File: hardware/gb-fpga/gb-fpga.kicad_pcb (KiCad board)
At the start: 4 copper layers, 80.1 x 78.6 mm, 136 parts, among them J1 USB_C_Receptacle_USB2.0, J2 Cartridge-32pin, J3 BAT+, J4 BAT-, J5 Conn_02x25_Counter_Clockwise, Q1 MBT3904DW1, SW1 Switch, U1 xc7s25ftgb196, U2 MX25R3235FZBxx1, U3 FT2232HQ, U4 LTC3555, U5 TLV61046ADB, U6 TXS0108E, U7 TXS0108E, U8 TXS0108E, U9 TXS0108E, X1 SG-8002JA

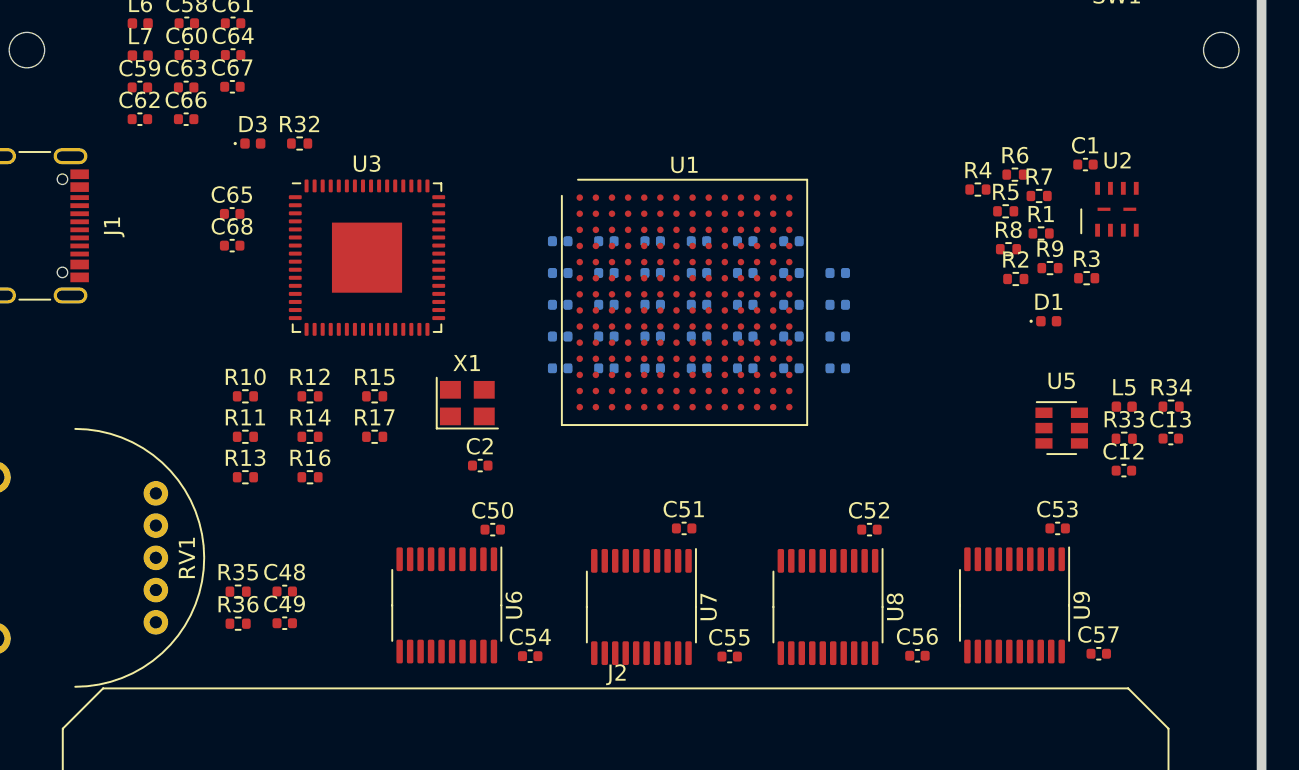
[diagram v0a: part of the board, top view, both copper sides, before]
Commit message: Layout some smaller groups
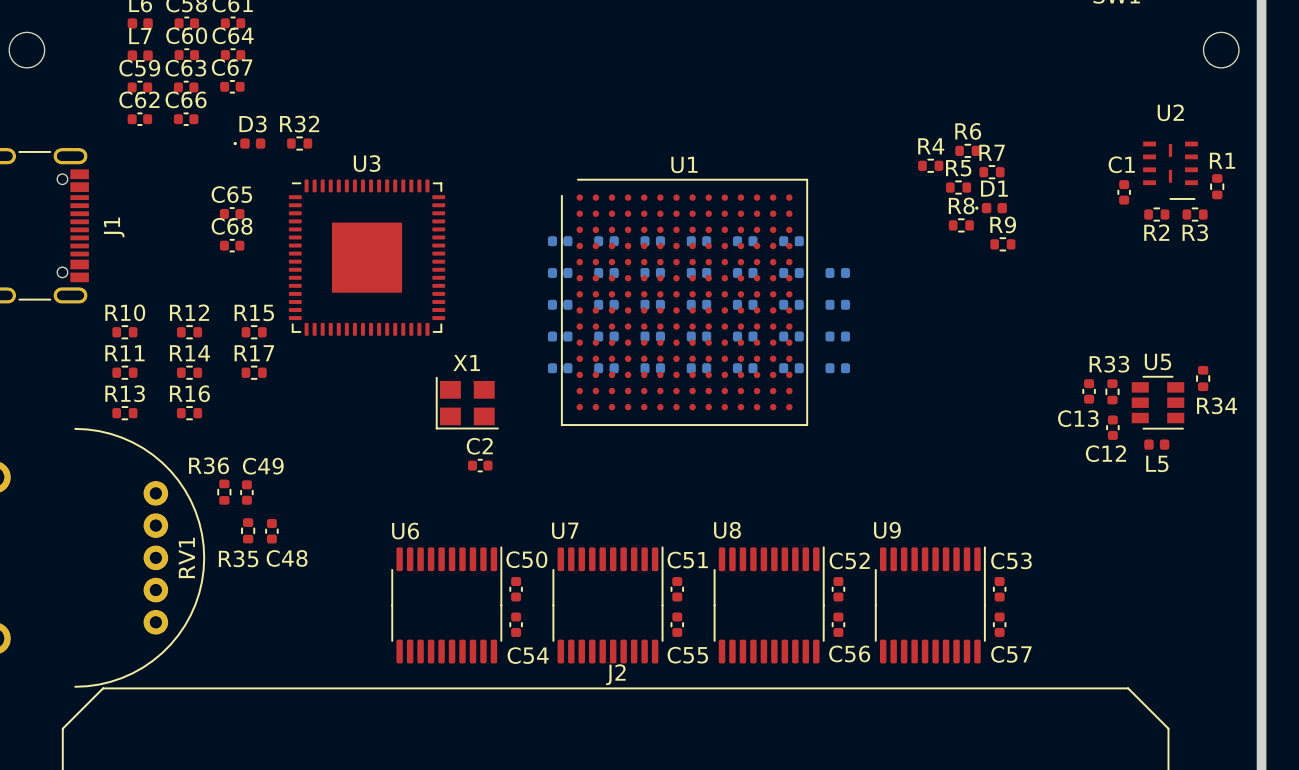
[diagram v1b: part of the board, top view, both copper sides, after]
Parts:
- moved R1 11.3 mm to (77.3, -57.6), turned to 270 degrees
- moved R2 9.62 mm to (73.6, -55.9), turned to 180 degrees
- moved R10 8.47 mm to (9.58, -48.6)
- moved R11 8.47 mm to (9.58, -46.1)
- moved R13 8.47 mm to (9.58, -43.6)
- moved R15 8.47 mm to (17.6, -48.6)
- moved R17 8.47 mm to (17.6, -46.1)
- moved R12 8.47 mm to (13.6, -48.6)
- moved R14 8.47 mm to (13.6, -46.1)
- moved R16 8.47 mm to (13.6, -43.6)
- moved C49 8.44 mm to (17.1, -38.6), turned to 270 degrees
- moved R36 8.20 mm to (15.8, -38.7), turned to 90 degrees
- moved R3 7.80 mm to (76.0, -55.9), turned to 180 degrees
- moved D1 7.79 mm to (63.5, -56.3)
- moved C57 6.41 mm to (63.9, -30.4), turned to 90 degrees
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
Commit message: Place more components
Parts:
- moved R11 26.0 mm to (22.6, -68.6)
- moved R13 26.0 mm to (22.6, -66.0)
- moved R14 26.0 mm to (26.6, -68.6)
- moved R10 26.0 mm to (22.6, -71.1)
- moved R12 26.0 mm to (26.6, -71.1)
- moved R15 26.0 mm to (30.7, -71.1)
- moved C63 20.7 mm to (30.0, -51.5), turned to 270 degrees
- moved C66 19.7 mm to (27.2, -47.8), turned to 270 degrees
- moved C67 16.8 mm to (30.5, -54.9)
- moved L6 15.6 mm to (14.7, -52.7), turned to 90 degrees
- moved C58 15.3 mm to (16.0, -52.7), turned to 270 degrees
- moved C10 14.7 mm to (9.60, -58.1), turned to 90 degrees
- moved C62 13.3 mm to (17.3, -50.3), turned to 270 degrees
- moved C59 13.0 mm to (17.3, -52.7), turned to 270 degrees
- moved R17 12.7 mm to (9.60, -55.9), turned to 270 degrees
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
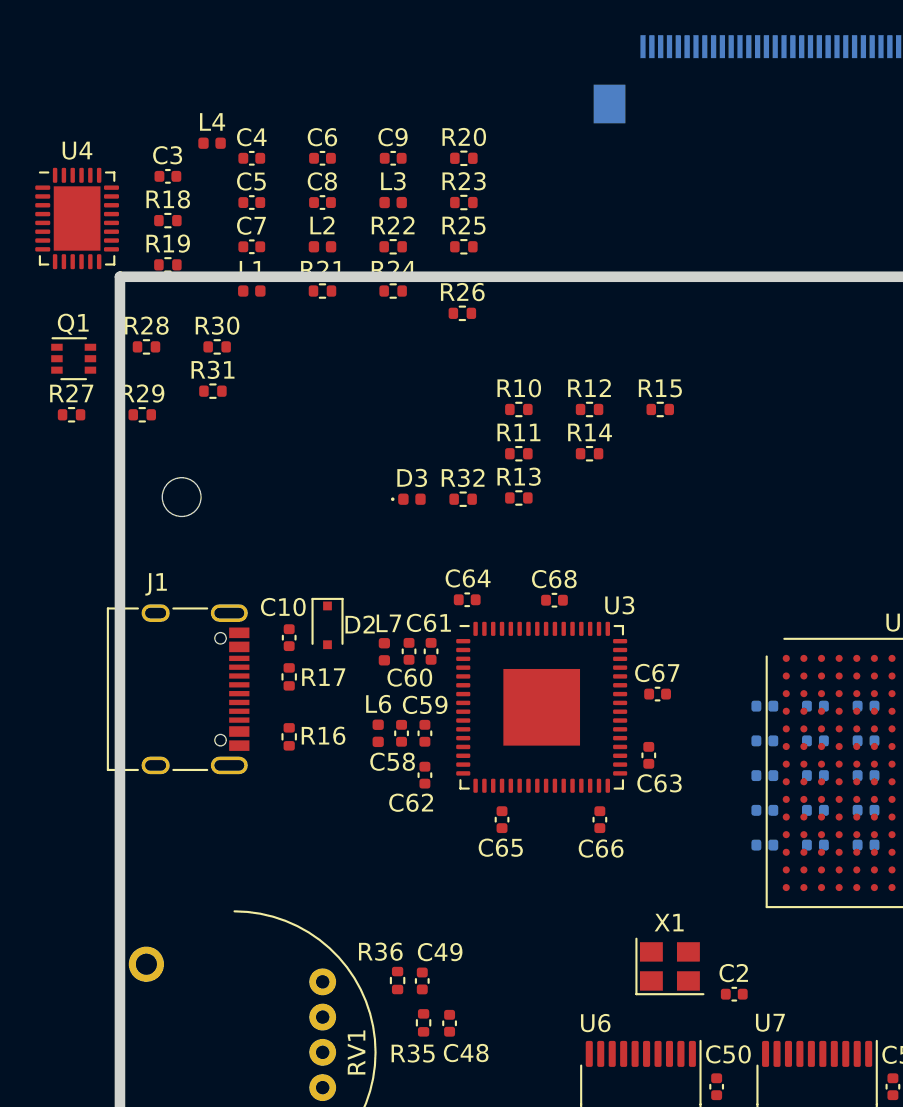
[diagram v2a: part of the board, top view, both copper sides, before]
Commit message: Place power components
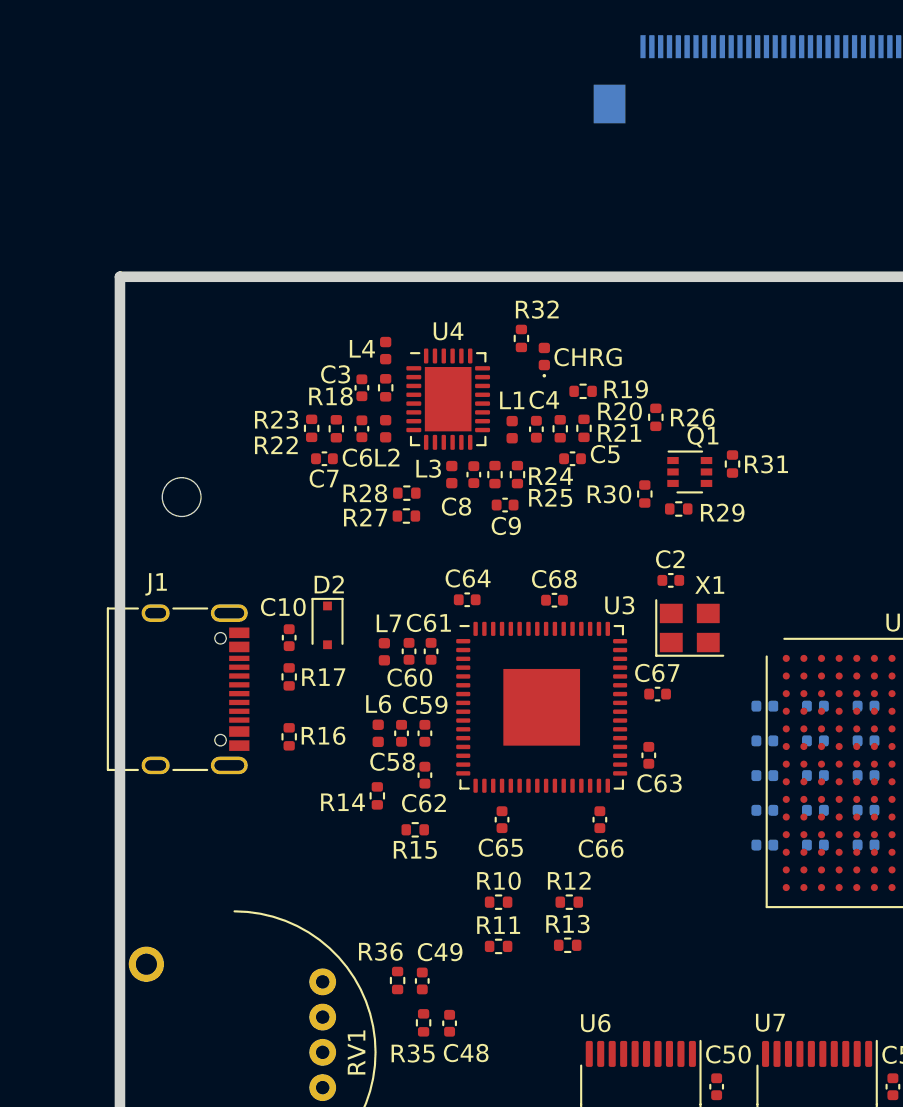
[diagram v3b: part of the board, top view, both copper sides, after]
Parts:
- moved Q1 35.5 mm to (32.3, -67.5)
- moved R29 30.9 mm to (31.7, -65.4)
- moved R31 29.8 mm to (34.8, -68.0), turned to 270 degrees
- moved R11 28.0 mm to (21.5, -40.6)
- moved R10 28.0 mm to (21.5, -43.1)
- moved R12 28.0 mm to (25.5, -43.1)
- moved R15 27.6 mm to (16.8, -47.2), turned to 180 degrees
- moved R30 25.7 mm to (29.8, -66.3), turned to 90 degrees
- moved R13 25.5 mm to (25.4, -40.7)
- moved R19 24.6 mm to (26.3, -72.1)
- moved C2 23.7 mm to (31.2, -61.4)
- moved U4 23.4 mm to (18.6, -71.7)
- moved C5 23.3 mm to (25.7, -68.3)
- moved R14 22.8 mm to (14.6, -49.1), turned to 270 degrees
- moved C4 22.3 mm to (23.6, -70.0), turned to 90 degrees
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- renumbered D3 to CHRG

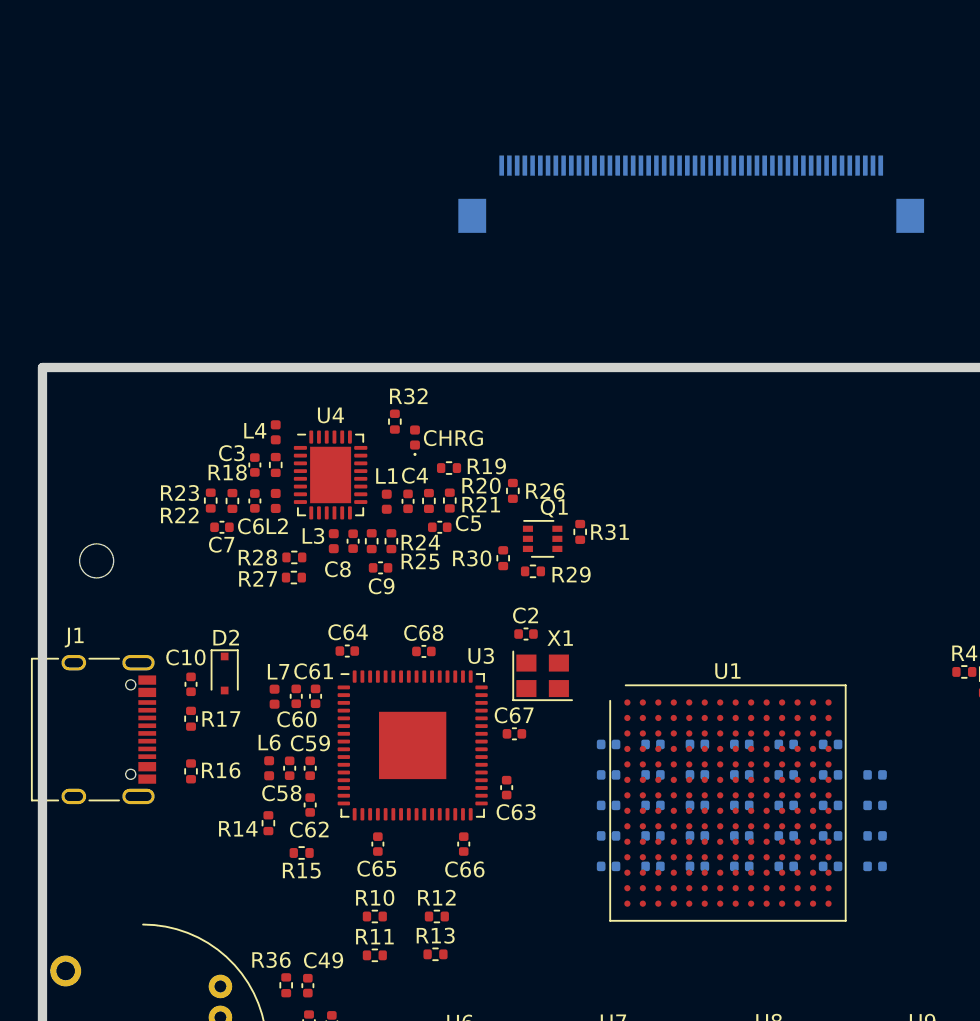
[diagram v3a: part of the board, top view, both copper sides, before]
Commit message: Fan out part of BGA
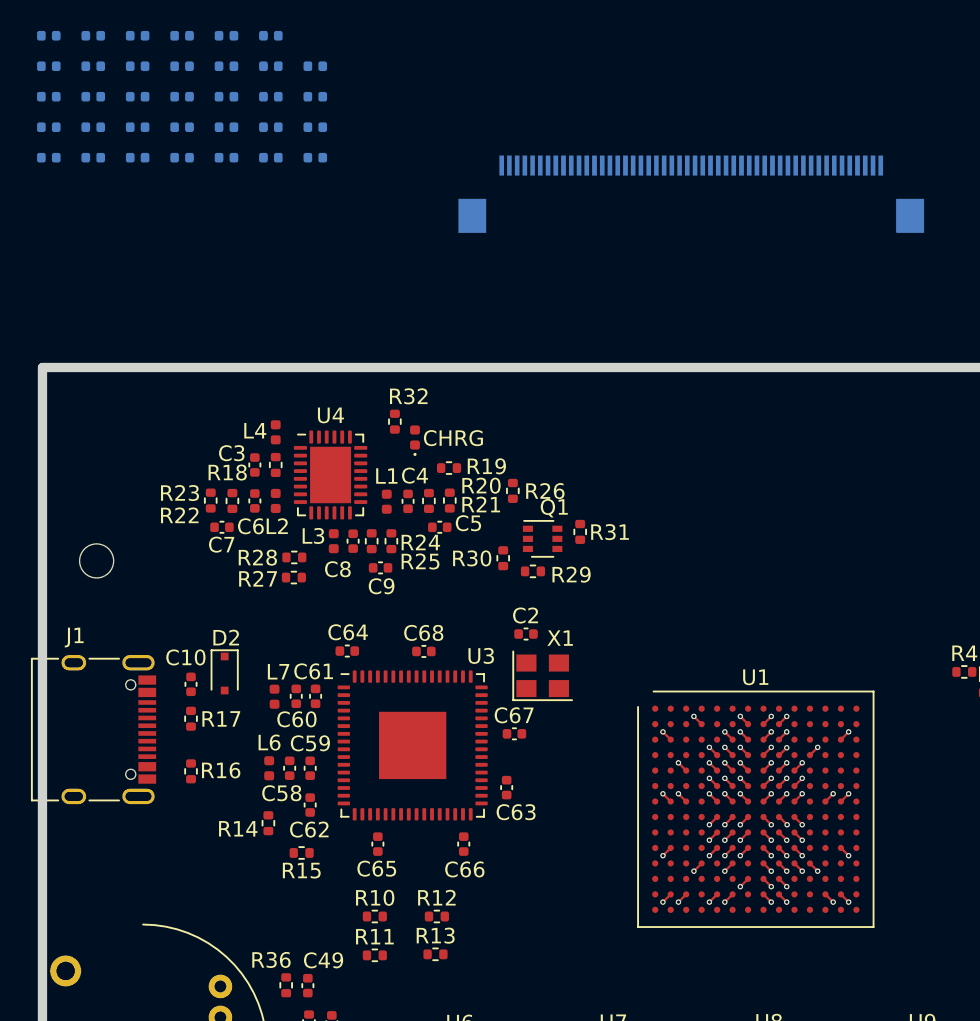
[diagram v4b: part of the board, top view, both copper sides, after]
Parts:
- moved C16 58.4 mm to (3.28, -92.2)
- moved C17 58.4 mm to (0.41, -96.1)
- moved C20 58.4 mm to (0.41, -98.1)
- moved C21 58.4 mm to (3.28, -96.1)
- moved C24 58.4 mm to (0.41, -100.0)
- moved C25 58.4 mm to (3.28, -98.1)
- moved C26 58.4 mm to (6.15, -96.1)
- moved C28 58.4 mm to (11.9, -92.2)
- moved C29 58.4 mm to (3.28, -100.0)
- moved C30 58.4 mm to (6.15, -98.1)
- moved C31 58.4 mm to (9.02, -96.1)
- moved C34 58.4 mm to (6.15, -100.0)
- moved C35 58.4 mm to (9.02, -98.1)
- moved C36 58.4 mm to (11.9, -96.1)
- moved C39 58.4 mm to (9.02, -100.0)
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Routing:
- net GND: track 0.00 -> 34.0 mm, vias 0 -> 48
- net +1V0: track 0.00 -> 9.19 mm, vias 0 -> 13
- net +3V3: track 0.00 -> 6.36 mm, vias 0 -> 9
- net +1V8: track 0.00 -> 4.24 mm, vias 0 -> 6
- added copper zone on In1.Cu, net GND

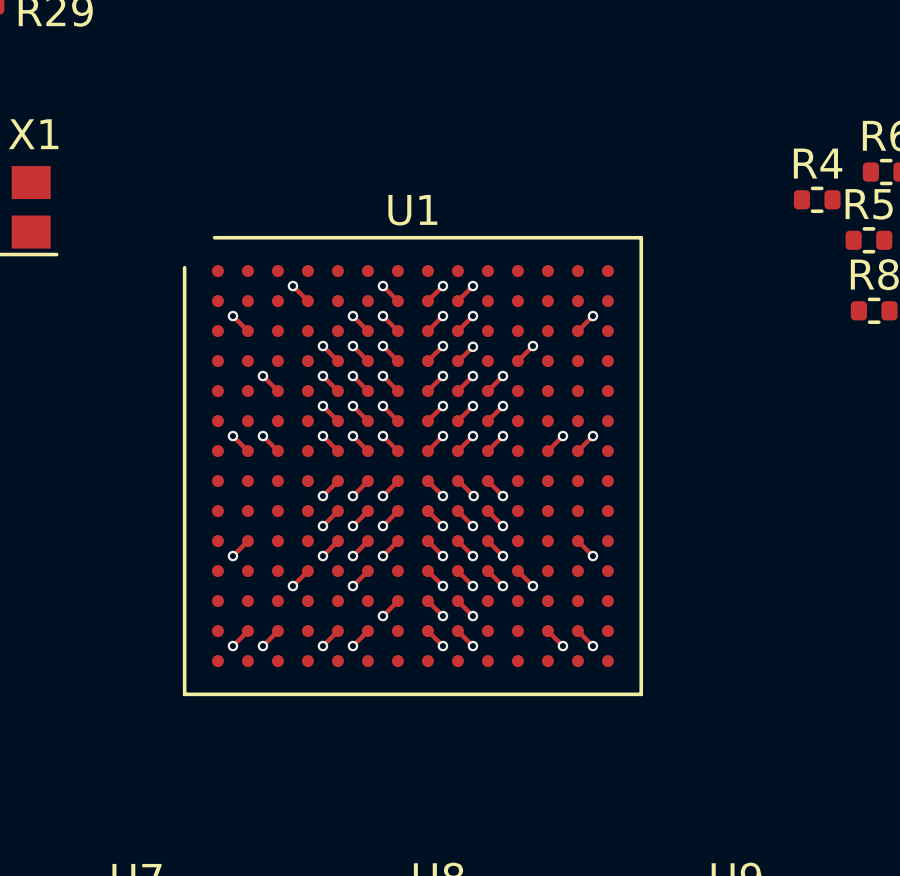
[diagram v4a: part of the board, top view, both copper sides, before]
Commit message: Fan out cartridge pins
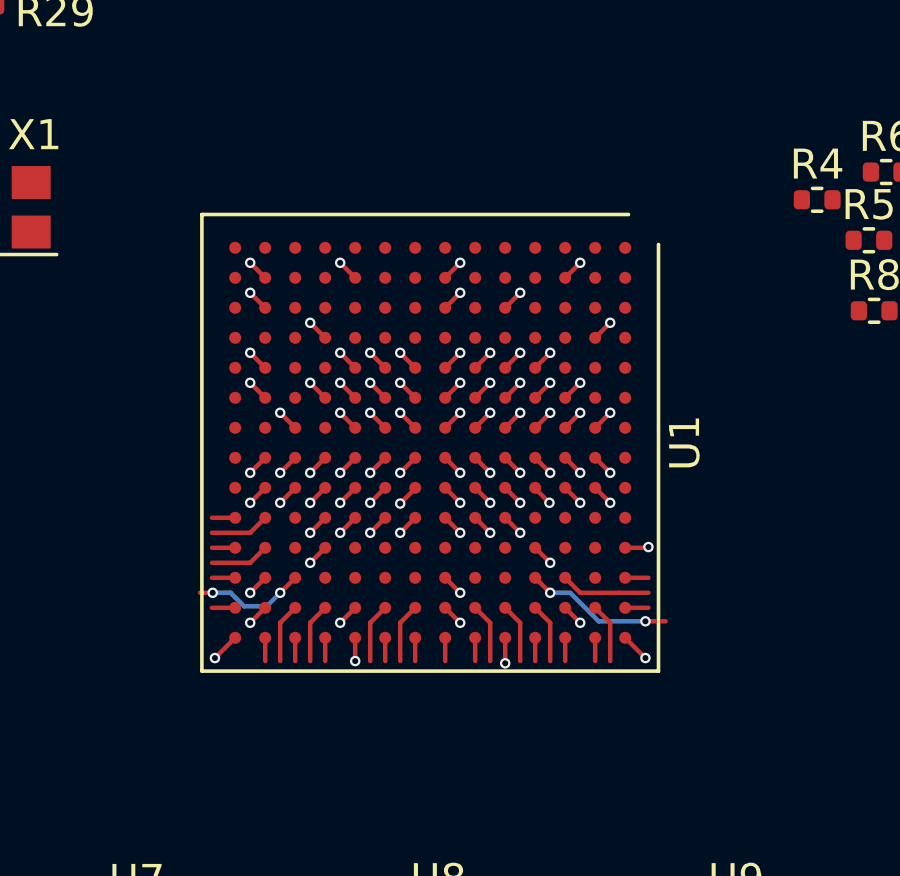
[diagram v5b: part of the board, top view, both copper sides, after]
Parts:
- moved U1 0.97 mm to (46.7, -50.8), turned to 270 degrees
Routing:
- net Net-(U1-PadD12): track 0.00 -> 4.95 mm, vias 0 -> 2
- net GND: track 34.0 -> 38.3 mm, vias 48 -> 53
- net Net-(U1-PadM12): track 0.00 -> 3.75 mm, vias 0 -> 2
- net Net-(U1-PadC12): track 0.00 -> 2.98 mm
- net Net-(U1-PadM13): track 0.00 -> 1.98 mm
- net Net-(U1-PadL13): track 0.00 -> 1.98 mm
- net Net-(U1-PadJ13): track 0.00 -> 1.98 mm
- net Net-(U1-PadH13): track 0.00 -> 1.98 mm
- net Net-(U1-PadF13): track 0.00 -> 1.98 mm
- net Net-(U1-PadE13): track 0.00 -> 1.98 mm
- net Net-(U1-PadD13): track 0.00 -> 1.98 mm
- net Net-(U1-PadB13): track 0.00 -> 1.98 mm
- net Net-(U1-PadN11): track 0.00 -> 1.98 mm
- net Net-(U1-PadN10): track 0.00 -> 1.98 mm
- net Net-(U1-PadN14): track 0.00 -> 0.78 mm
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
